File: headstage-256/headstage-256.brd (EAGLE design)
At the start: 32 x 32 mm, 300 parts, among them J2 MMCX-J-P-H-ST-SM1/U.FL-R-SMT(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, J4 PINHD-2X5+4DF40-HEAD, J5 5041940270, U1 OPA170, U10 NRF24L01QFN, U11 CAT4016_QFN, U12 CAT4016_QFN, U13 TPL0501_UQFN, U14 TPL0501_UQFN, U15 MICROSD_473093751, U16 10M08SAM15317G, U17 Si8487DB, U18 MAX17048_WLP, U19 BNO055, U2 OPA170, U20 TPS61202, U21 RHD2064_BGA, U22 RHD2064_BGA, U23 TS4231, U24 TS4231, U25 LT3463, U26 ASCO-50.000MHZ-EK-T3, U27 TS4231, U28 TLV70733, U29 TS4231, U3 INA826, U30 RHD2064_BGA, U31 RHD2064_BGA, U32 MIC23150, U33 TS4231, U34 TS4231, U35 TPS8268180, U4 INA826, U5 DAC5311, U6 DAC5311, U7 DS90UB913A_WQFN, Y1 FW1600008, Y2 ECS-.327-12.5-1210-TR

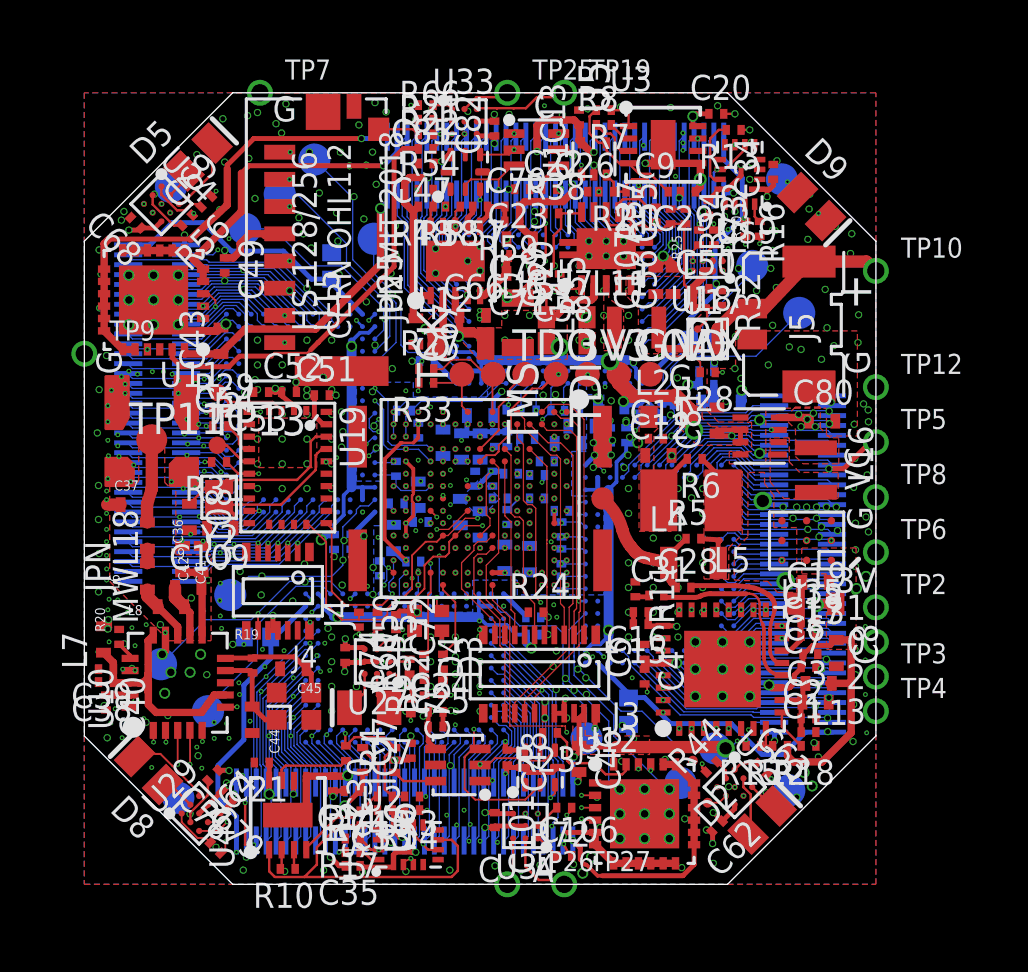
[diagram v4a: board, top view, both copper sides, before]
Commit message: Minor fixes following headstage-256 assembly
- Corrected 0201 LED package
- Moved a couple passives apart to reduce shorts
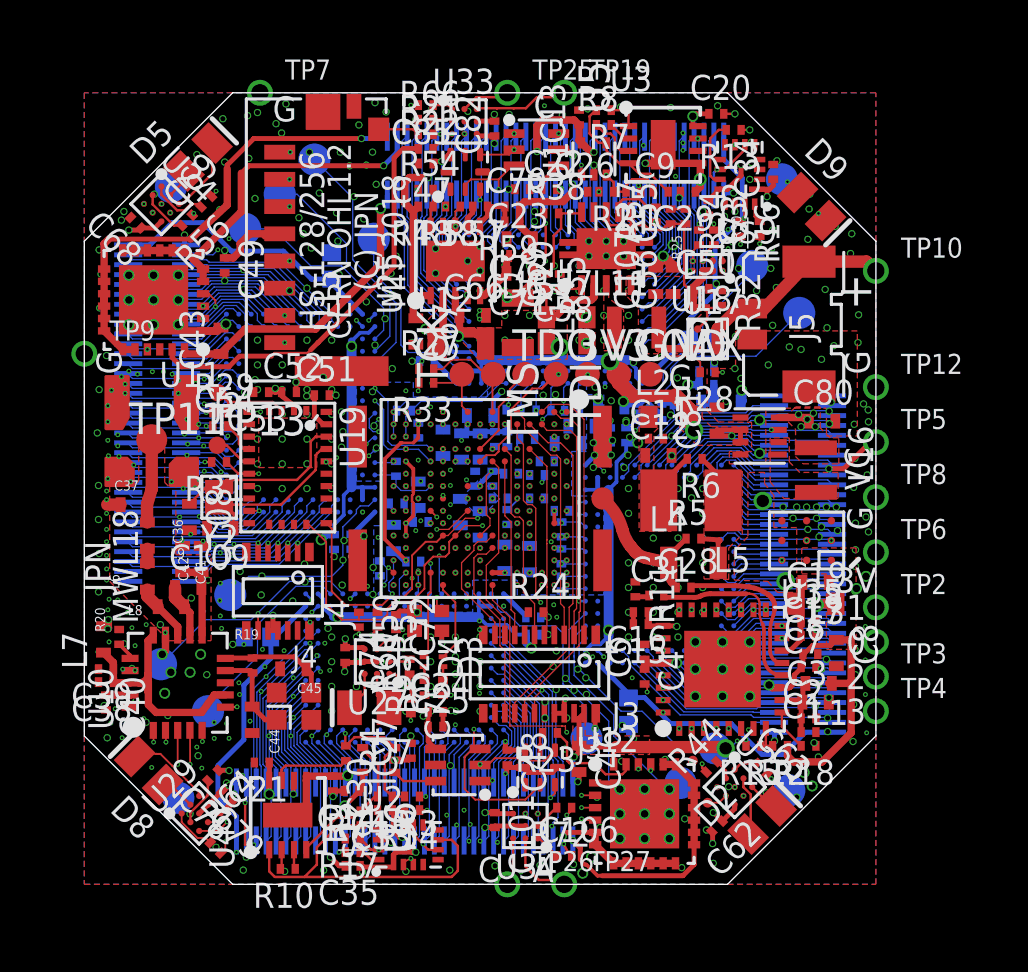
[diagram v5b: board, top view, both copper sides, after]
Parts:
- moved R16 0.20 mm to (10.5, 10.5)
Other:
- board text added: "MIT 2018"
- board text removed: "JPN MIT 2018"
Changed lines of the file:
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@@
 <setting verticaltext="up"/>
 </settings>
-<grid distance="0.05" unitdist="mm" unit="mm" style="lines" multiple="1" display="yes" altdistance="0.025" altunitdist="inch" altunit="inch"/>
+<grid distance="0.1" unitdist="mm" unit="mm" style="lines" multiple="1" display="yes" altdistance="0.025" altunitdist="inch" altunit="inch"/>
 <layers>
 <layer number="1" name="Top" color="4" fill="1" visible="yes" active="yes"/>
@@
 <layer number="3" name="GND" color="11" fill="1" visible="yes" active="yes"/>
 <layer number="4" name="VCC" color="1" fill="4" visible="yes" active="yes"/>
-<layer number="5" name="DRoute/AGND" color="4" fill="4" visible="no" active="yes"/>
+<layer number="5" name="DRoute/AGND" color="4" fill="4" visible="yes" active="yes"/>
 <layer number="6" name="Route6" color="1" fill="8" visible="no" active="no"/>
 <layer number="7" name="Route7" color="4" fill="8" visible="no" active="no"/>
@@
 <layer number="21" name="tPlace" color="7" fill="1" visible="no" active="yes"/>
 <layer number="22" name="bPlace" color="7" fill="1" visible="no" active="yes"/>
-<layer number="23" name="tOrigins" color="15" fill="1" visible="yes" active="yes"/>
-<layer number="24" name="bOrigins" color="15" fill="1" visible="no" active="yes"/>
+<layer number="23" name="tOrigins" color="15" fill="1" visible="no" active="yes"/>
+<layer number="24" name="bOrigins" color="15" fill="1" visible="yes" active="yes"/>
 <layer number="25" name="tNames" color="7" fill="1" visible="no" active="yes"/>
 <layer number="26" name="bNames" color="7" fill="1" visible="no" active="yes"/>
 <layer number="27" name="tValues" color="7" fill="1" visible="no" active="yes"/>
 <layer number="28" name="bValues" color="7" fill="1" visible="no" active="yes"/>
-<layer number="29" name="tStop" color="7" fill="3" visible="yes" active="yes"/>
+<layer number="29" name="tStop" color="7" fill="3" visible="no" active="yes"/>
 <layer number="30" name="bStop" color="7" fill="6" visible="no" active="yes"/>
 <layer number="31" name="tCream" color="7" fill="4" visible="no" active="yes"/>
@@
 <layer number="37" name="tTest" color="7" fill="1" visible="no" active="yes"/>
 <layer number="38" name="bTest" color="7" fill="1" visible="no" active="yes"/>
-<layer number="39" name="tKeepout" color="4" fill="11" visible="yes" active="yes"/>
+<layer number="39" name="tKeepout" color="4" fill="11" visible="no" active="yes"/>
 <layer number="40" name="bKeepout" color="1" fill="11" visible="no" active="yes"/>
 <layer number="41" name="tRestrict" color="4" fill="10" visible="no" active="yes"/>
@@
 <text x="5.9" y="-9.15" size="1.016" layer="21" font="vector" ratio="18" align="center">J3</text>
 <text x="-5.8" y="-5.05" size="1.016" layer="21" font="vector" ratio="18" rot="R90" align="center">J4</text>
-<text x="-7.1" y="10" size="1" layer="21" font="vector" ratio="18" rot="R90" align="center">HS-128/256</text>
+<text x="-6.8" y="10" size="1" layer="21" font="vector" ratio="18" rot="R90" align="center">HS-128/256</text>
 <text x="-5.7" y="10" size="0.95" layer="21" font="vector" ratio="18" rot="R90" align="center">CERN OHL1.2</text>
-<text x="-3.6" y="10.6" size="0.95" layer="21" font="vector" ratio="18" rot="R90" align="center">JPN MIT 2018
-</text>
+<text x="-4.6" y="10" size="0.95" layer="21" font="vector" ratio="18" rot="R90" align="center">(C) JPN</text>
 <text x="2.55" y="-15.4" size="1.016" layer="21" font="vector" ratio="18" align="center">A</text>
 <text x="2.6" y="15.5" size="1.016" layer="21" font="vector" ratio="18" align="center">C</text>
@@
 <text x="-5.6" y="11.3" size="1.016" layer="22" font="vector" ratio="18" rot="SMR225" align="center">OUT</text>
 <text x="-11.25" y="11.65" size="1.016" layer="22" font="vector" ratio="18" rot="SMR225" align="center">G</text>
+<text x="-3.5" y="10" size="0.95" layer="21" font="vector" ratio="18" rot="R90" align="center">MIT 2018</text>
 </plain>
 <attributes>
@@
 <attribute name="PARTNO" value="TPL0501-100RSER" x="47.7" y="-4.7" size="1.778" layer="27" rot="R90" display="off"/>
 </element>
-<element name="R16" library="jonnew" package="0201T" value="10k" x="10.725" y="10.5" rot="R270"/>
+<element name="R16" library="jonnew" package="0201T" value="10k" x="10.525" y="10.5" rot="R270"/>
 <element name="C23" library="jonnew" package="0201T" value="1uF" x="1.7" y="12.1" rot="R180">
 <attribute name="PARTNO" value="CL03A105MP3ZSNH" x="20.8" y="72.1" size="1.778" layer="27" rot="R180" display="off"/>
@@
 <wire x1="10.675" y1="11.5" x2="10.675" y2="10.925" width="0.0762" layer="1"/>
 <wire x1="10.675" y1="10.925" x2="10.675" y2="10.85" width="0.0762" layer="1"/>
-<wire x1="10.675" y1="10.85" x2="10.725" y2="10.8" width="0.0762" layer="1"/>
+<wire x1="10.675" y1="10.85" x2="10.525" y2="10.8" width="0.0762" layer="1"/>
 <wire x1="7.41828125" y1="10.925" x2="10.675" y2="10.925" width="0.0762" layer="2"/>
 <wire x1="1.8" y1="9.525" x2="3.337778125" y2="11.062778125" width="0.0762" layer="2"/>
@@
 <contactref element="R52" pad="2"/>
 <contactref element="D3" pad="2"/>
-<wire x1="-1.5" y1="-7.75" x2="-1.5" y2="-7.3" width="0.1" layer="1"/>
+<wire x1="-1.5" y1="-7.75" x2="-1.5" y2="-7.2" width="0.1" layer="1"/>
 </signal>
 <signal name="N$93">
@@
 <contactref element="D4" pad="2"/>
 <wire x1="-2.25" y1="-7.75" x2="-2.25" y2="-7.26665" width="0.1" layer="1"/>
-<wire x1="-2.25" y1="-7.26665" x2="-2.26665" y2="-7.3" width="0.1" layer="1"/>
+<wire x1="-2.25" y1="-7.26665" x2="-2.26665" y2="-7.2" width="0.1" layer="1"/>
 </signal>
 <signal name="JTAGEN">
@@
 <wire x1="-1.5" y1="-3.9" x2="-1.5" y2="-4.1" width="0.0762" layer="1"/>
 <wire x1="-1.5" y1="-4.1" x2="-1" y2="-4.6" width="0.0762" layer="1"/>
-<wire x1="-1" y1="-4.6" x2="-1" y2="-6.2" width="0.0762" layer="1"/>
-<wire x1="-1" y1="-6.2" x2="-1.5" y2="-6.7" width="0.0762" layer="1"/>
+<wire x1="-1" y1="-6.3" x2="-1.5" y2="-6.8" width="0.0762" layer="1"/>
+<wire x1="-1" y1="-4.6" x2="-1" y2="-6.3" width="0.0762" layer="1"/>
 </signal>
 <signal name="STATUS_A">
@@
 <wire x1="-2" y1="-3.4" x2="-2" y2="-4.2" width="0.0762" layer="1"/>
 <wire x1="-2" y1="-4.2" x2="-2.1" y2="-4.3" width="0.0762" layer="1"/>
-<wire x1="-2.1" y1="-6.53335" x2="-2.26665" y2="-6.7" width="0.0762" layer="1"/>
-<wire x1="-2.1" y1="-4.3" x2="-2.1" y2="-6.53335" width="0.0762" layer="1"/>
+<wire x1="-2.1" y1="-6.63335" x2="-2.26665" y2="-6.8" width="0.0762" layer="1"/>
+<wire x1="-2.1" y1="-4.3" x2="-2.1" y2="-6.63335" width="0.0762" layer="1"/>
 </signal>
 <signal name="NCONFIG">
@@
 <via x="10.3" y="15.15" extent="1-4" drill="0.2"/>
 <via x="11.825" y="10.45" extent="1-4" drill="0.2"/>
-<via x="10.725" y="9.875" extent="1-4" drill="0.1"/>
+<via x="10.525" y="9.875" extent="1-4" drill="0.1"/>
 <via x="10.025" y="9.7" extent="1-4" drill="0.1"/>
-<wire x1="10.725" y1="10.2" x2="10.725" y2="9.875" width="0.1" layer="1"/>
+<wire x1="10.525" y1="10.2" x2="10.525" y2="9.875" width="0.1" layer="1"/>
 <via x="10.9" y="14.5" extent="1-4" drill="0.2"/>
 <via x="-14.075" y="-5.625" extent="1-4" drill="0.1"/>

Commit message: headstage-256 rev 1.1
- Should be ready for speedy
- 8 layer board should fix radio-freq isolation issue on previous
version
- Other small circuit modifications and fixes
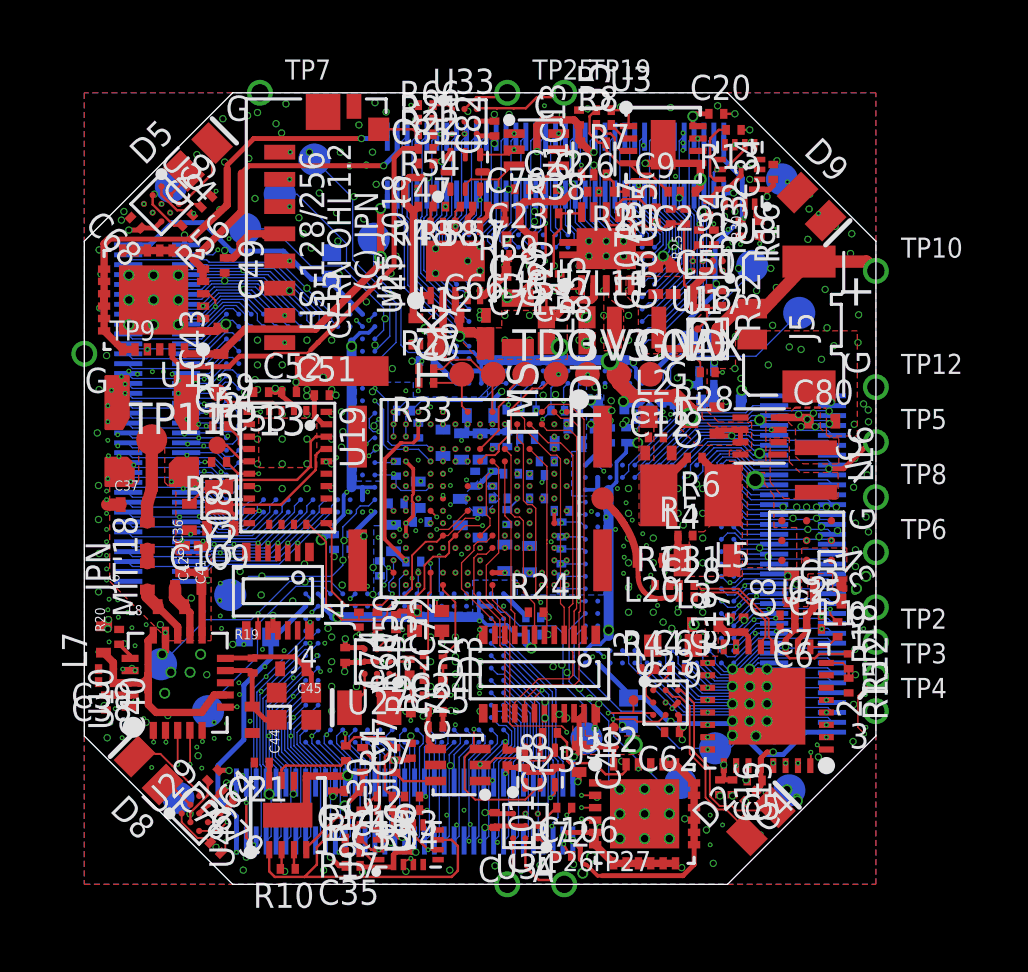
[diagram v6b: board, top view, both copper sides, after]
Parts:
- added L20: BLM15PX121SN1D, jonnew:0402T
- U8, U9: value (none) -> DG509B
- moved C16 7.77 mm to (9.70, -12.1), turned to 270 degrees
- moved C15 7.56 mm to (10.2, -12.1), turned to 270 degrees
- moved C5 6.84 mm to (11.1, -11.8), turned to 180 degrees
- moved C4 6.47 mm to (10.9, -12.4), turned to 225 degrees
- moved C19 6.00 mm to (7.80, -6.35), turned to 180 degrees
- moved C63 5.27 mm to (8.00, -7.30), turned to 0 degrees
- moved TP28 4.86 mm to (5.41, -9.66), turned to 45 degrees
- moved R18 4.85 mm to (14.4, -5.69), turned to 270 degrees
- moved L3 4.77 mm to (9.10, -5.50), turned to 0 degrees
- moved R44 4.70 mm to (6.80, -7.30), turned to 0 degrees
- moved R15 4.56 mm to (14.9, -7.96), turned to 270 degrees
- moved U23 4.41 mm to (7.50, -8.65), turned to 0 degrees
- moved R12 4.40 mm to (14.9, -6.99), turned to 270 degrees
- moved C62 4.22 mm to (7.76, -9.85), turned to 180 degrees
- moved C1 4.18 mm to (13.5, -5.67)
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- renumbered U$22 to U9, U$9 to U8
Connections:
- net N$44 renamed DOUT_P
- net N$45 renamed DOUT_N
- new net PREFILT: L20.1, L4.1, R5.1
- net !LIPO_ALRT: now also U16.E7; no longer U16.A2
- net DIN0: now also U16.B11; no longer U16.D7
- net DIN1: now also U16.B12; no longer U16.B8
- net DIN10: now also U16.B8; no longer U16.B12
- net DIN11: now also U16.B7; no longer U16.D11
- net DIN2: now also U16.D11; no longer U16.C8
- net DIN3: now also U16.A13; no longer U16.A9
- net DIN4: now also U16.B13; no longer U16.E7
- net DIN5: now also U16.A14; no longer U16.E9
- net DIN6: now also U16.B14; no longer U16.D10
- net DIN7: now also U16.B15; no longer U16.E10
- net DIN8: now also U16.A9; no longer U16.A11
- net DIN9: now also U16.A7; no longer U16.B11
- net HSYNC: now also U16.A5; no longer U16.A13
- net LIPO_QSTRT: now also U16.A2; no longer U16.A3
- net PCLK: now also U16.C8; no longer U16.A14
- net SERDES_EN: now also U16.D7; no longer U16.B4
- net SERDES_GPIO0: now also U16.E9; no longer U16.B6
- net SERDES_GPIO1: now also U16.D10; no longer U16.A5
- net SERDES_GPIO2: now also U16.E10; no longer U16.B7
- net SERDES_GPIO3: now also U16.A11; no longer U16.A7
- net SERDES_SCL: now also U16.B4; no longer U16.B14
- net SERDES_SDA: now also U16.B6; no longer U16.B15
- net SIGOUT: now also L20.2; no longer L4.1, R5.1
- net VSYNC: now also U16.A3; no longer U16.B13
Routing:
- net PCLK: track 10.5 -> 22.0 mm
- net SERDES_GPIO0: track 16.4 -> 27.1 mm
- net DIN10: track 8.70 -> 19.3 mm
- net DIN8: track 7.88 -> 18.2 mm
- net VSYNC: track 10.6 -> 20.0 mm
- net DIN9: track 8.65 -> 17.9 mm
- net DIN11: track 10.3 -> 19.5 mm
- net HSYNC: track 9.30 -> 18.4 mm
- net SERDES_GPIO1: track 16.4 -> 25.3 mm
- net SERDES_GPIO2: track 17.0 -> 24.6 mm, vias 2 -> 3
- net SERDES_SCL: track 11.7 -> 18.5 mm
- net N$25: track 1.28 -> 7.84 mm
- net SERDES_SDA: track 12.1 -> 17.9 mm
- net N$26: track 2.48 -> 7.79 mm
- net LH_ENV1: track 14.3 -> 9.90 mm
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- added copper zone on layer 5, net +3V3
- added copper zone on layer 7, net AGND
- added copper zone on layer 2, net GND
- added copper zone on layer 4, net GND
- added copper zone on layer 6, net GND
- added copper zone on layer 7, net GND
- added copper zone on layer 1, net N$50
- added copper zone on layer 5, net N$69
- removed copper zone on layer 4, net +3V3
- removed copper zone on layer 5, net AGND
- removed copper zone on layer 3, net GND
- removed copper zone on layer 5, net GND
- removed copper zone on layer 2, net N$69
- removed copper zone on layer 4, net N$69
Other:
- board text added: "(C)JPN"
- board text added: "JPN MIT'18"
- board text added: "r1.1"
- board text removed: "JPN MWL18"
- board text removed: "r1.0"

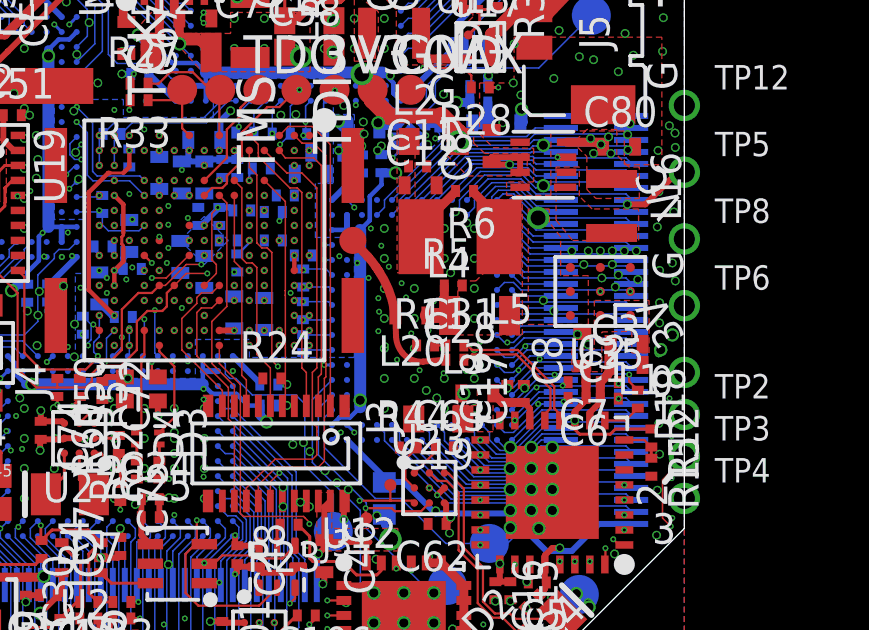
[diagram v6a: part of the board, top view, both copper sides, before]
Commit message: Minore changes to headstage-256
- But restrict layer on top around high frequency lines to widen out
spacing to top level ground layer. Provides more accurate micro-strip
characteristics.
- Gerbers updated.
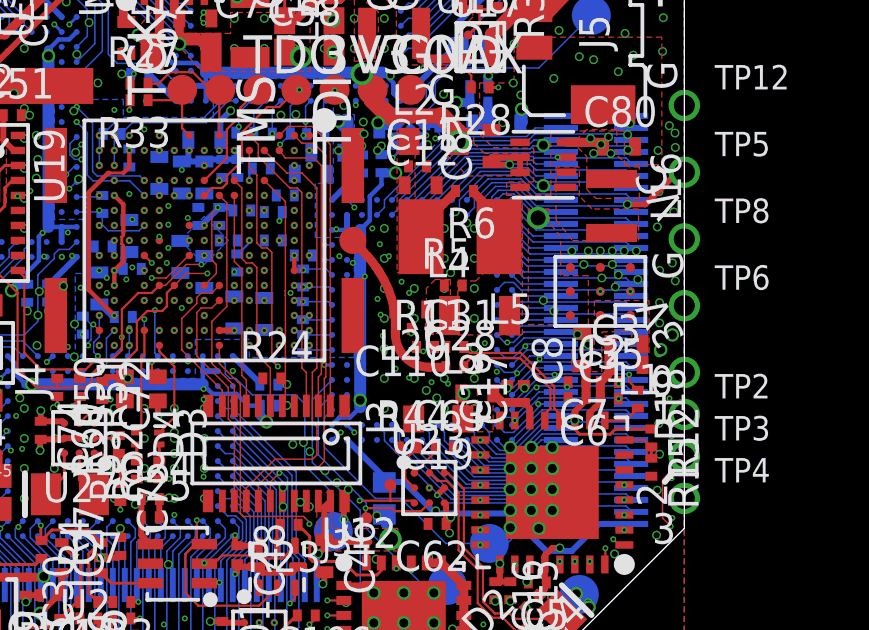
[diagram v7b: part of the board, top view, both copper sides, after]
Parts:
- added C110: 68pF, NP0 (DNP), jonnew:0201T
- moved C28 0.25 mm to (8.35, -4.62)
- moved L20 0.20 mm to (6.90, -2.70)
- moved C31 0.05 mm to (8.35, -3.95)
- moved R11 0.05 mm to (7.38, -3.95)
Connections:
- net GND: now also C110.2
- net PREFILT: now also C110.1
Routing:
- net PREFILT: track 1.81 -> 0.25 mm
- net GND: vias 450 -> 451
- added copper zone on layer 1, net PREFILT
